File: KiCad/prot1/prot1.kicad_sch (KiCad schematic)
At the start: 67 parts, among them U1 LM393

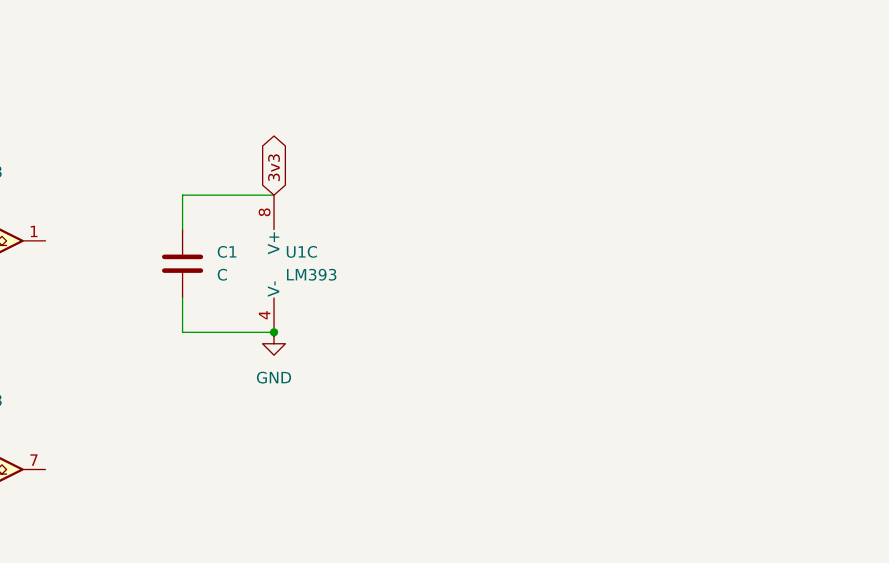
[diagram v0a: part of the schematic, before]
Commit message: ALSフットプリント作成
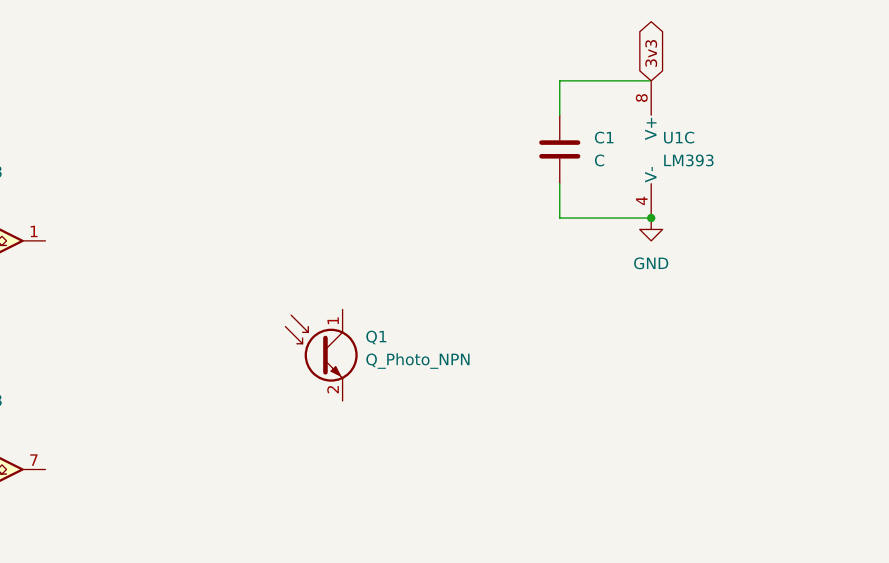
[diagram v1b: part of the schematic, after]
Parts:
- added Q1: Q_Photo_NPN, symbol Device:Q_Photo_NPN
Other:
- moved on the sheet: C1, U1C
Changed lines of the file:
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@@
 	)
 	(junction
-		(at 127 66.04)
+		(at 168.91 53.34)
 		(diameter 0)
 		(color 0 0 0 0)
@@
 	(wire
 		(pts
-			(xy 116.84 54.61) (xy 116.84 50.8)
+			(xy 158.75 41.91) (xy 158.75 38.1)
 		)
 		(stroke
@@
 	(wire
 		(pts
-			(xy 116.84 66.04) (xy 127 66.04)
+			(xy 158.75 53.34) (xy 168.91 53.34)
 		)
 		(stroke
@@
 	(wire
 		(pts
-			(xy 116.84 50.8) (xy 127 50.8)
+			(xy 158.75 38.1) (xy 168.91 38.1)
 		)
 		(stroke
@@
 	(wire
 		(pts
-			(xy 116.84 62.23) (xy 116.84 66.04)
+			(xy 158.75 49.53) (xy 158.75 53.34)
 		)
 		(stroke
@@
 	(global_label "3v3"
 		(shape bidirectional)
-		(at 127 50.8 90)
+		(at 168.91 38.1 90)
 		(fields_autoplaced yes)
 		(effects
@@
 		)
 		(property "Intersheetrefs" "${INTERSHEET_REFS}"
-			(at 127 43.3169 90)
+			(at 168.91 30.6169 90)
 			(hide yes)
 			(show_name no)
@@
 		)
 		(property "3v3" ""
-			(at 130.8418 50.8 90)
+			(at 172.7518 38.1 90)
 			(hide yes)
 			(show_name no)
@@
 	(symbol
 		(lib_id "power:GND")
-		(at 127 66.04 0)
+		(at 168.91 53.34 0)
 		(unit 1)
 		(body_style 1)
@@
 		(fields_autoplaced yes)
 		(property "Reference" "#PWR01"
-			(at 127 72.39 0)
+			(at 168.91 59.69 0)
 			(hide yes)
 			(show_name no)
@@
 		)
 		(property "Value" "GND"
-			(at 127 71.12 0)
+			(at 168.91 58.42 0)
 			(show_name no)
 			(do_not_autoplace no)
@@
 		)
 		(property "Footprint" ""
-			(at 127 66.04 0)
+			(at 168.91 53.34 0)
 			(hide yes)
 			(show_name no)
@@
 		)
 		(property "Datasheet" ""
-			(at 127 66.04 0)
+			(at 168.91 53.34 0)
 			(hide yes)
 			(show_name no)
@@
 		)
 		(property "Description" "Power symbol creates a global label with name \"GND\" , ground"
-			(at 127 66.04 0)
+			(at 168.91 53.34 0)
 			(hide yes)
 			(show_name no)
@@
 	)
 	(symbol
+		(lib_id "Device:Q_Photo_NPN")
+		(at 132.08 68.58 0)
+		(unit 1)
+		(body_style 1)
+		(exclude_from_sim no)
+		(in_bom yes)
+		(on_board yes)
+		(in_pos_files yes)
+		(dnp no)
+		(fields_autoplaced yes)
+		(property "Reference" "Q1"
+			(at 137.16 66.5606 0)
+			(show_name no)
+			(do_not_autoplace no)
+			(effects
+				(font
+					(size 1.27 1.27)
+				)
+				(justify left)
+			)
+		)
+		(property "Value" "Q_Photo_NPN"
+			(at 137.16 69.1006 0)
+			(show_name no)
+			(do_not_autoplace no)
+			(effects
+				(font
+					(size 1.27 1.27)
+				)
+				(justify left)
+			)
+		)
+		(property "Footprint" ""
+			(at 137.16 66.04 0)
+			(hide yes)
+			(show_name no)
+			(do_not_autoplace no)
+			(effects
+				(font
+					(size 1.27 1.27)
+				)
+			)
+		)
+		(property "Datasheet" ""
+			(at 132.08 68.58 0)
+			(hide yes)
+			(show_name no)
+			(do_not_autoplace no)
+			(effects
+				(font
+					(size 1.27 1.27)
+				)
+			)
+		)
+		(property "Description" "NPN phototransistor, collector/emitter"
+			(at 132.08 68.58 0)
+			(hide yes)
+			(show_name no)
+			(do_not_autoplace no)
+			(effects
+				(font
+					(size 1.27 1.27)
+				)
+			)
+		)
+		(pin "1"
+		)
+		(pin "2"
+		)
+		(instances
+			(project "prot1"
+				(path "/fa6edba8-a662-468c-9fac-cb6e7a59dfa8"
+					(reference "Q1")
+					(unit 1)
+				)
+			)
+		)
+	)
+	(symbol
 		(lib_id "Device:R")
 		(at 154.94 266.7 180)
@@
 	(symbol
 		(lib_id "Device:C")
-		(at 116.84 58.42 0)
+		(at 158.75 45.72 0)
 		(unit 1)
 		(body_style 1)
@@
 		(fields_autoplaced yes)
 		(property "Reference" "C1"
-			(at 120.65 57.1499 0)
+			(at 162.56 44.4499 0)
 			(show_name no)
 			(do_not_autoplace no)
@@
 		)
 		(property "Value" "C"
-			(at 120.65 59.6899 0)
+			(at 162.56 46.9899 0)
 			(show_name no)
 			(do_not_autoplace no)
@@
 		)
 		(property "Footprint" ""
-			(at 117.8052 62.23 0)
+			(at 159.7152 49.53 0)
 			(hide yes)
 			(show_name no)
@@
 		)
 		(property "Datasheet" ""
-			(at 116.84 58.42 0)
+			(at 158.75 45.72 0)
 			(hide yes)
 			(show_name no)
@@
 		)
 		(property "Description" "Unpolarized capacitor"
-			(at 116.84 58.42 0)
+			(at 158.75 45.72 0)
 			(hide yes)
 			(show_name no)
@@
 	(symbol
 		(lib_id "Comparator:LM393")
-		(at 129.54 58.42 0)
+		(at 171.45 45.72 0)
 		(unit 3)
 		(body_style 1)
@@
 		(fields_autoplaced yes)
 		(property "Reference" "U1"
-			(at 128.27 57.1499 0)
+			(at 170.18 44.4499 0)
 			(show_name no)
 			(do_not_autoplace no)
@@
 		)
 		(property "Value" "LM393"
-			(at 128.27 59.6899 0)
+			(at 170.18 46.9899 0)
 			(show_name no)
 			(do_not_autoplace no)
@@
 		)
 		(property "Footprint" ""
-			(at 129.54 58.42 0)
+			(at 171.45 45.72 0)
 			(hide yes)
 			(show_name no)
@@
 		)
 		(property "Datasheet" "http://www.ti.com/lit/ds/symlink/lm393.pdf"
-			(at 129.54 58.42 0)
+			(at 171.45 45.72 0)
 			(hide yes)
 			(show_name no)
@@
 		)
 		(property "Description" "Low-Power, Low-Offset Voltage, Dual Comparators, DIP-8/SOIC-8/TO-99-8"
-			(at 129.54 58.42 0)
+			(at 171.45 45.72 0)
 			(hide yes)
 			(show_name no)
